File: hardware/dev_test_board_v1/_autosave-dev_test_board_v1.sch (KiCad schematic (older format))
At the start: 39 parts

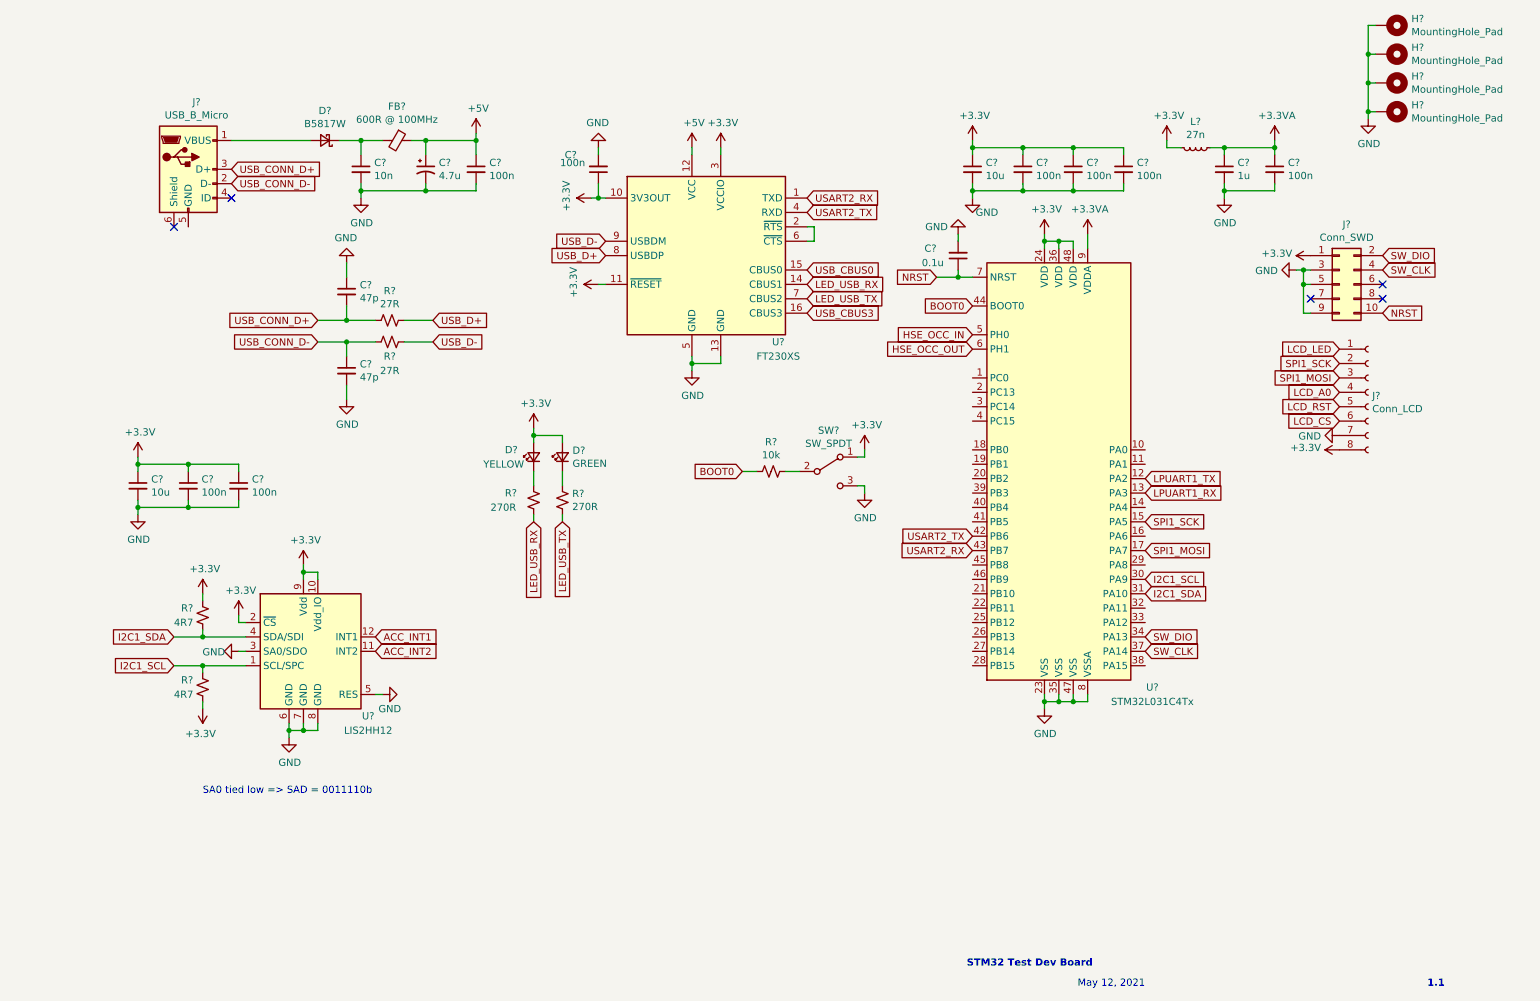
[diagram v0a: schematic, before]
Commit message: All needed pins assigned.
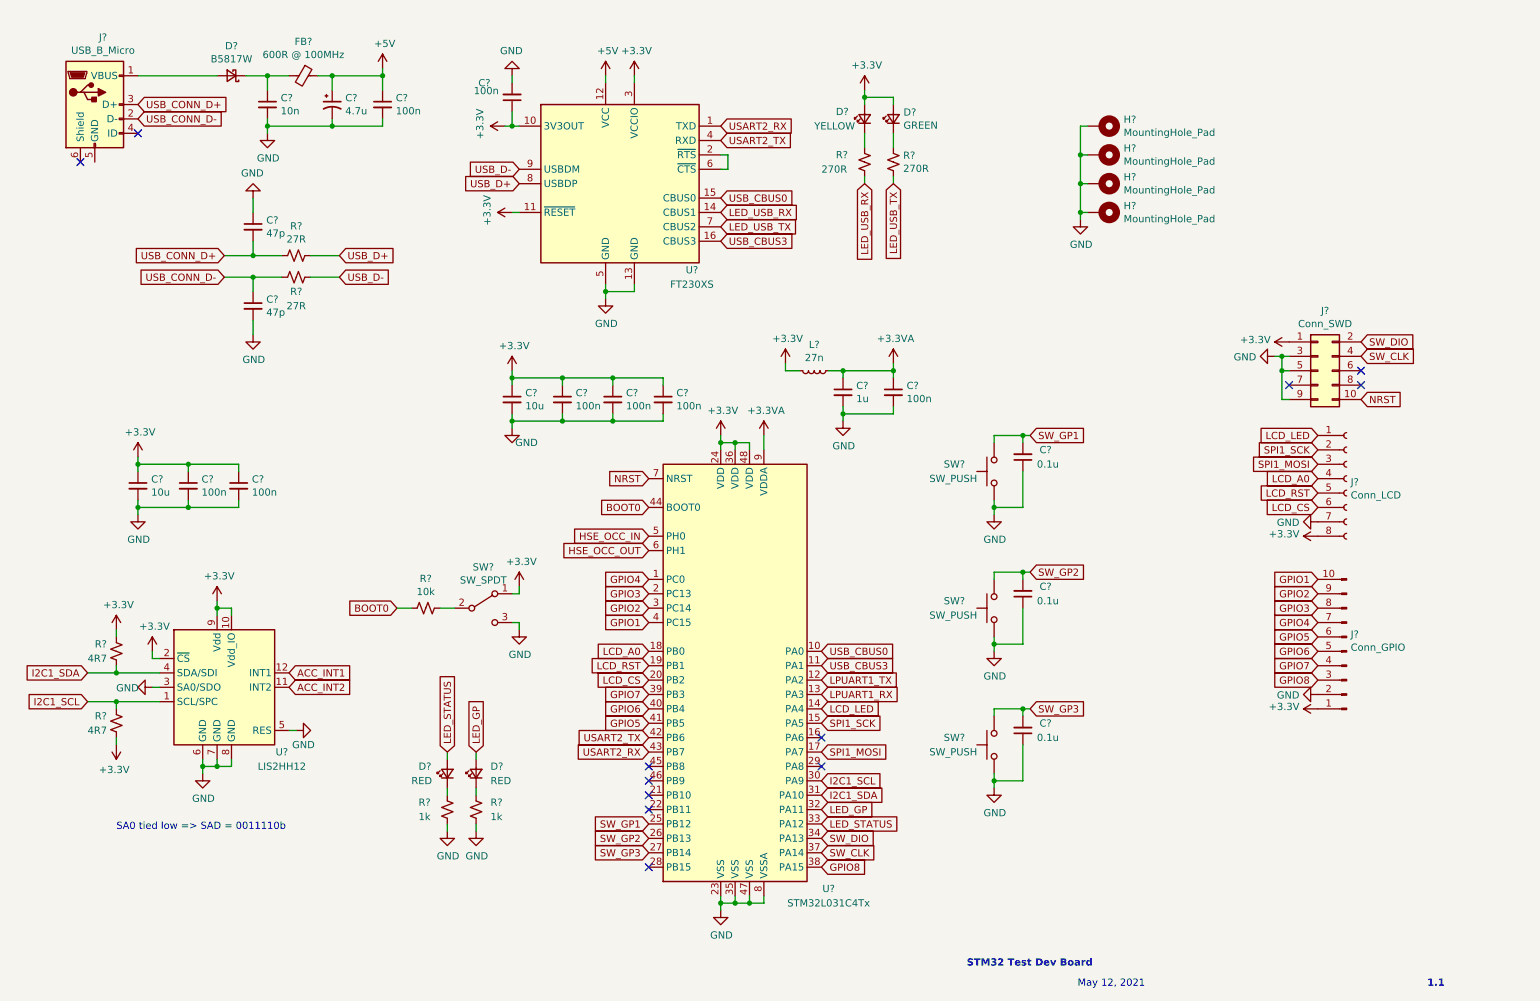
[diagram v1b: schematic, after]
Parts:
- added C? (x2): 0.1u, symbol Device:C_Small
- added D? (x2): RED, symbol Device:LED_Small
- added J?: Conn_GPIO, symbol Connector:Conn_01x10_Male
- added R? (x2): 1k, symbol Device:R_Small_US
- added SW? (x3): SW_PUSH, symbol Switch:SW_Push
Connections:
- net +3V3: now also J?.1 (Pin_1)
- net GND: now also C?.1, C?.1, C?.1, J?.2 (Pin_2), R?.2, R?.2, SW?.1, SW?.1, SW?.1; no longer C?.2
- net LCD_A0: now also U?.18 (PB0)
- net LCD_CS: now also U?.20 (PB2)
- net LCD_LED: now also U?.14 (PA4)
- net LCD_RST: now also U?.19 (PB1)
- net NRST: no longer C?.1
- net USB_CBUS0: now also U?.10 (PA0)
- net USB_CBUS3: now also U?.11 (PA1)
- net GPIO4: now reaches U?.1 (PC0)
- net GPIO4: now also J?.7 (Pin_7)
- net GPIO3: now reaches U?.2 (PC13)
- net GPIO3: now also J?.8 (Pin_8)
- net SW_GP1: now reaches U?.25 (PB12)
- net SW_GP1: now also C?.2, SW?.2
- net SW_GP2: now reaches U?.26 (PB13)
- net SW_GP2: now also C?.2, SW?.2
- net SW_GP3: now reaches U?.27 (PB14)
- net SW_GP3: now also C?.2, SW?.2
- net GPIO2: now reaches U?.3 (PC14)
- net GPIO2: now also J?.9 (Pin_9)
- net LED_GP: now reaches U?.32 (PA11)
- net LED_GP: now also D?.2 (A)
- net LED_STATUS: now reaches U?.33 (PA12)
- net LED_STATUS: now also D?.2 (A)
- net GPIO8: now reaches U?.38 (PA15)
- net GPIO8: now also J?.3 (Pin_3)
- net GPIO7: now reaches U?.39 (PB3)
- net GPIO7: now also J?.4 (Pin_4)
- net GPIO1: now reaches U?.4 (PC15)
- net GPIO1: now also J?.10 (Pin_10)
- net GPIO6: now reaches U?.40 (PB4)
- net GPIO6: now also J?.5 (Pin_5)
- net GPIO5: now reaches U?.41 (PB5)
- net GPIO5: now also J?.6 (Pin_6)
- new net: D?.1 (K), R?.1 (x2)
- no-connect marks 5 -> 12
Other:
- moved on the sheet: C?, D?, FB?, H?, J?, L?, R?, SW?, U?
